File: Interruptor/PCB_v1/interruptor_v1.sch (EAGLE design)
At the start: 31 parts, among them IC1 LM1117MPX-3.3, SW1 CI-11, U2 TCLD1000, X1 MAB5SH

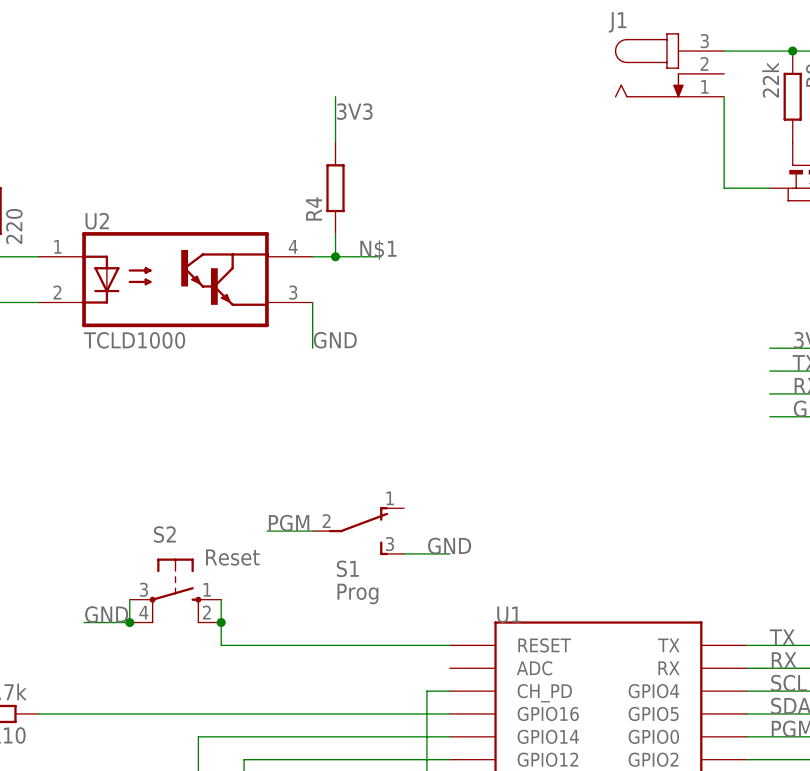
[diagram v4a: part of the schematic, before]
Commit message: placed tname/bname silkscreen
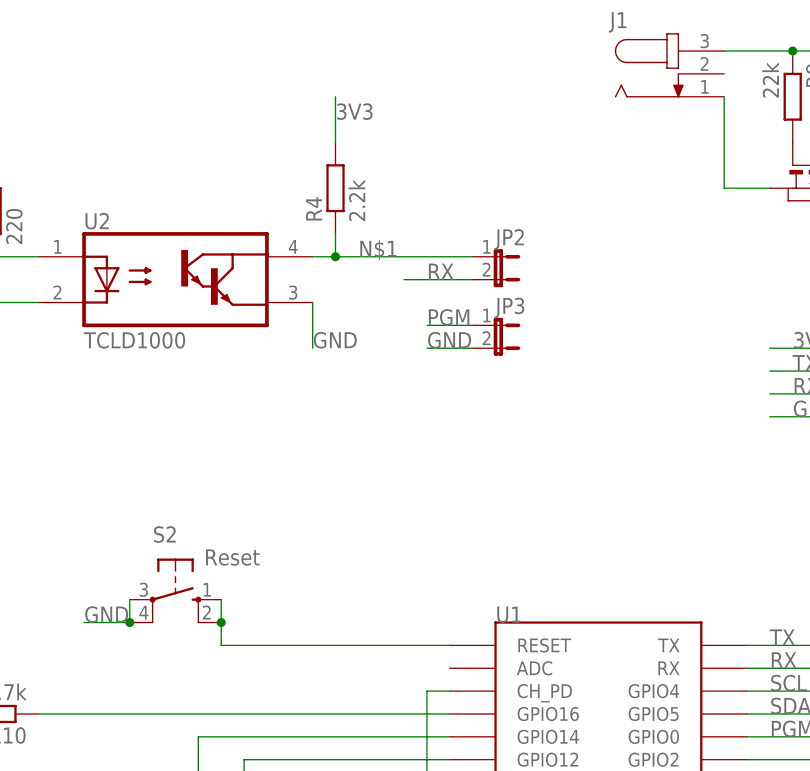
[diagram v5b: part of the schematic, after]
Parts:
- removed S1: Prog, switch:TL36YO
- added JP2, JP3: (no value), jumper:JP1E
- R4: value (none) -> 2.2k
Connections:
- net GND: now also JP3.2; no longer S1.S
- net N$1: now also JP2.1
- net PGM: now also JP3.1; no longer S1.P
- net RX: now also JP2.2
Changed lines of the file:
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@@
 <part name="R2" library="resistor" deviceset="R-EU_" device="M0805" value="4.7k"/>
 <part name="R3" library="resistor" deviceset="R-EU_" device="M0805" value="4.7k"/>
-<part name="R4" library="resistor" deviceset="R-EU_" device="M0805"/>
+<part name="R4" library="resistor" deviceset="R-EU_" device="M0805" value="2.2k"/>
 <part name="R5" library="resistor" deviceset="R-EU_" device="M0805" value="220"/>
 <part name="D1" library="diode" deviceset="DIODE-" device="DO214AA"/>
@@
 <part name="U$2" library="fibre" deviceset="OPF372" device="OPF372"/>
 <part name="R1" library="resistor" deviceset="R-EU_" device="M0805" value="15R 1/2W"/>
-<part name="S1" library="switch" deviceset="TL36YO" device="" value="Prog"/>
 <part name="S2" library="switch-omron" deviceset="10-XX" device="" value="Reset"/>
 <part name="SV2" library="con-lstb" deviceset="MA04-1" device="" value="UART"/>
@@
 <part name="R9" library="resistor" deviceset="R-EU_" device="M0805" value="22k"/>
 <part name="R10" library="resistor" deviceset="R-EU_" device="M0805" value="4.7k"/>
+<part name="JP2" library="jumper" deviceset="JP1E" device=""/>
+<part name="JP3" library="jumper" deviceset="JP1E" device=""/>
 </parts>
 <sheets>
@@
 <instance part="U$2" gate="G$1" x="205.74" y="63.5"/>
 <instance part="R1" gate="G$1" x="205.74" y="76.2" rot="R90"/>
-<instance part="S1" gate="BEF1" x="99.06" y="88.9" rot="R270"/>
 <instance part="S2" gate="1" x="78.74" y="81.28" rot="R270"/>
 <instance part="SV2" gate="1" x="160.02" y="104.14" rot="R180"/>
@@
 <instance part="R9" gate="G$1" x="147.32" y="137.16" rot="R270"/>
 <instance part="R10" gate="G$1" x="58.42" y="68.58" rot="R180"/>
+<instance part="JP2" gate="A" x="114.3" y="119.38" rot="R270"/>
+<instance part="JP3" gate="A" x="114.3" y="111.76" rot="R270"/>
 </instances>
 <busses>
@@
 <wire x1="152.4" y1="104.14" x2="144.78" y2="104.14" width="0.1524" layer="91"/>
 <label x="147.32" y="104.14" size="1.778" layer="95"/>
+</segment>
+<segment>
+<pinref part="JP2" gate="A" pin="2"/>
+<wire x1="111.76" y1="116.84" x2="104.14" y2="116.84" width="0.1524" layer="91"/>
+<label x="106.68" y="116.84" size="1.778" layer="95"/>
 </segment>
 </net>
@@
 </segment>
 <segment>
-<pinref part="S1" gate="BEF1" pin="S"/>
-<wire x1="104.14" y1="86.36" x2="109.22" y2="86.36" width="0.1524" layer="91"/>
-<label x="106.68" y="86.36" size="1.778" layer="95"/>
-</segment>
-<segment>
 <pinref part="S2" gate="1" pin="P1"/>
 <pinref part="S2" gate="1" pin="P"/>
@@
 <junction x="162.56" y="127"/>
 </segment>
+<segment>
+<pinref part="JP3" gate="A" pin="2"/>
+<wire x1="111.76" y1="109.22" x2="106.68" y2="109.22" width="0.1524" layer="91"/>
+<label x="106.68" y="109.22" size="1.778" layer="95"/>
+</segment>
 </net>
 <net name="N$1" class="0">
@@
 <wire x1="96.52" y1="119.38" x2="96.52" y2="121.92" width="0.1524" layer="91"/>
 <label x="99.06" y="119.38" size="1.778" layer="95"/>
-<wire x1="96.52" y1="119.38" x2="101.6" y2="119.38" width="0.1524" layer="91"/>
 <junction x="96.52" y="119.38"/>
+<pinref part="JP2" gate="A" pin="1"/>
+<wire x1="96.52" y1="119.38" x2="111.76" y2="119.38" width="0.1524" layer="91"/>
 </segment>
 </net>
@@
 </segment>
 <segment>
-<pinref part="S1" gate="BEF1" pin="P"/>
-<wire x1="93.98" y1="88.9" x2="88.9" y2="88.9" width="0.1524" layer="91"/>
-<label x="88.9" y="88.9" size="1.778" layer="95"/>
-</segment>
-</net>
+<pinref part="JP3" gate="A" pin="1"/>
+<wire x1="111.76" y1="111.76" x2="106.68" y2="111.76" width="0.1524" layer="91"/>
+<label x="106.68" y="111.76" size="1.778" layer="95"/>
+</segment>
+</net>
